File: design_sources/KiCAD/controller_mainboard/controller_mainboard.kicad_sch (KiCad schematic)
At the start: 34 parts, among them J1 XT-90, J10 01x08_2.54mm _socket, J11 2P_screw_term, J12 2P_screw_term, J13 2P_screw_term, J14 2P_screw_term, J2 XT-60, J24 XT-60, J25 XT-60, J3 USB_C_Receptacle_USB2.0_16P, J4 01x08_2.54mm _socket, J5 01x08_2.54mm _socket, J6 01x08_2.54mm _socket, J7 02x18_2.54mm_socket, J8 Conn_01x10_2.54mm_socket, J9 01x08_2.54mm _socket, Q1 2N7002, U12 USBLC6-4SC6

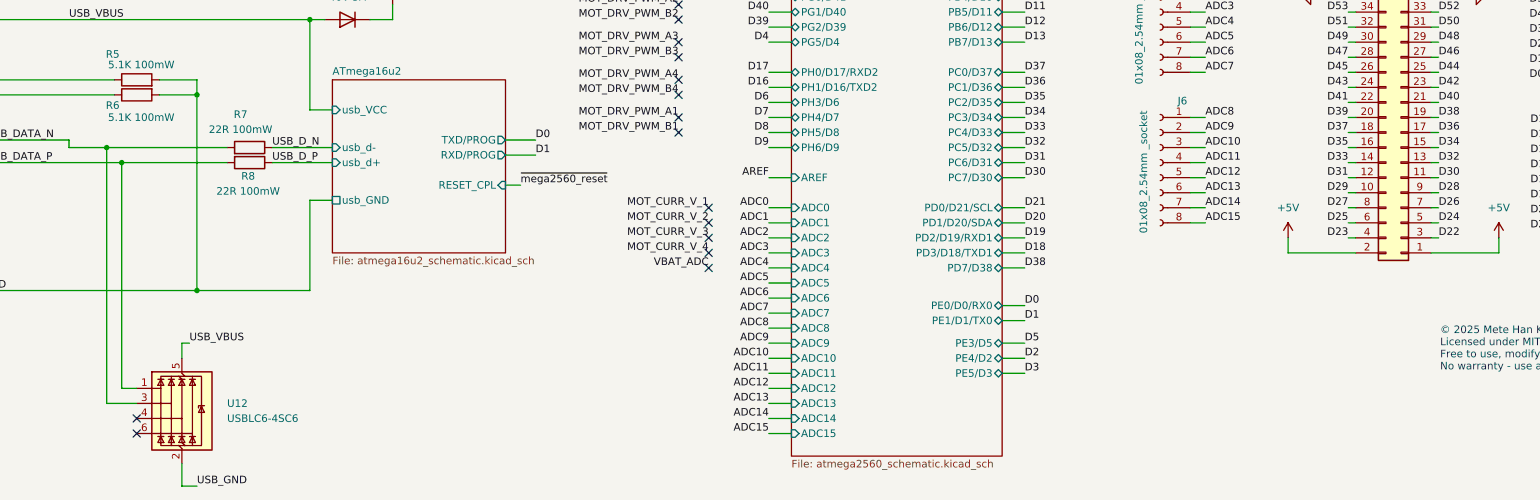
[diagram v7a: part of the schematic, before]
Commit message: Major PCB layout progress, motor drivers are routed and placed. PCB dimensions set, started ATMEGA2560 layout. Slight schematic fixes.
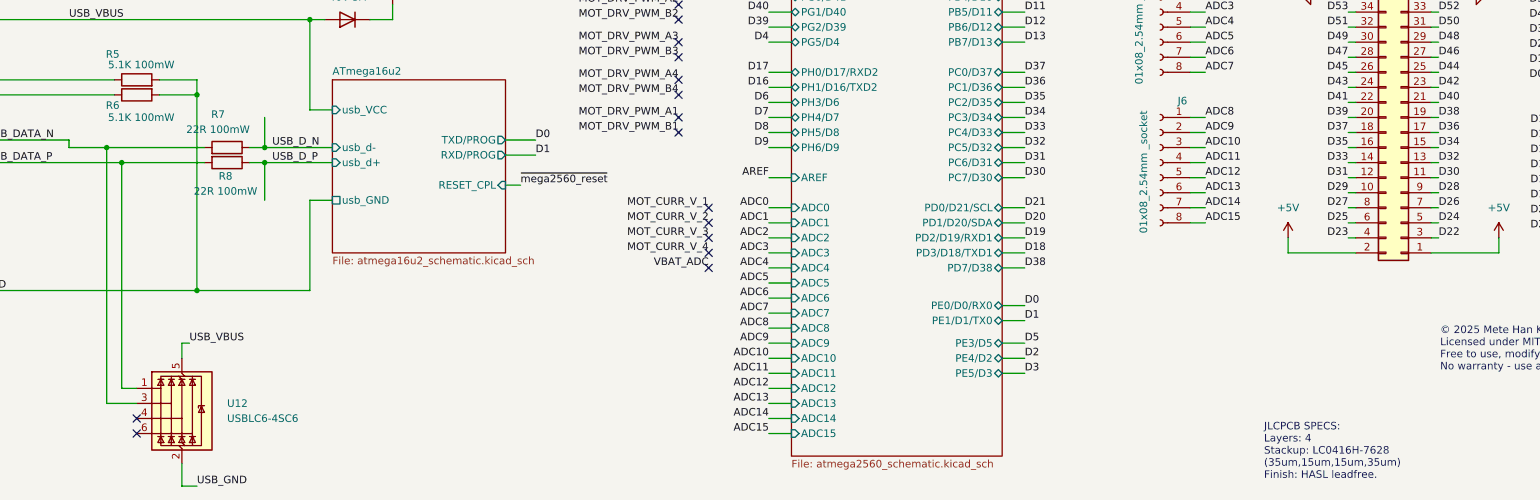
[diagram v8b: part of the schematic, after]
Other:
- note added: "JLCPCB SPECS: Layers: 4 Stackup: LC0416H-7628 (35um,15um,15um,35um) Finish: HASL leadfree."
- moved on the sheet: R7, R8
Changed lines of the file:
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@@
 		)
 	)
+	(text "JLCPCB SPECS:\nLayers: 4 \nStackup: LC0416H-7628\n(35um,15um,15um,35um)\nFinish: HASL leadfree."
+		(exclude_from_sim no)
+		(at 270.256 261.112 0)
+		(effects
+			(font
+				(size 1.27 1.27)
+			)
+			(justify left top)
+		)
+	)
 	(text "Emergency stop\nconnector"
 		(exclude_from_sim no)
@@
 	)
 	(junction
+		(at 101.6 214.63)
+		(diameter 0)
+		(color 0 0 0 0)
+	)
+	(junction
 		(at 90.17 238.76)
 		(diameter 0)
@@
 	)
 	(junction
+		(at 101.6 217.17)
+		(diameter 0)
+		(color 0 0 0 0)
+	)
+	(junction
 		(at 271.78 168.91)
 		(diameter 0)
@@
 	(wire
 		(pts
-			(xy 77.47 217.17) (xy 95.25 217.17)
+			(xy 77.47 217.17) (xy 91.44 217.17)
 		)
 		(stroke
@@
 	(wire
 		(pts
-			(xy 102.87 214.63) (xy 113.03 214.63)
+			(xy 101.6 214.63) (xy 113.03 214.63)
 		)
 		(stroke
@@
 	(wire
 		(pts
+			(xy 101.6 217.17) (xy 113.03 217.17)
+		)
+		(stroke
+			(width 0)
+			(type default)
+		)
+	)
+	(wire
+		(pts
 			(xy 306.07 38.1) (xy 309.88 38.1)
 		)
@@
 	(wire
 		(pts
+			(xy 101.6 209.55) (xy 101.6 214.63)
+		)
+		(stroke
+			(width 0)
+			(type default)
+		)
+	)
+	(wire
+		(pts
 			(xy 29.21 236.22) (xy 29.21 247.65)
 		)
@@
 	(wire
 		(pts
-			(xy 102.87 217.17) (xy 113.03 217.17)
+			(xy 229.87 214.63) (xy 226.06 214.63)
 		)
 		(stroke
@@
 	(wire
 		(pts
-			(xy 229.87 214.63) (xy 226.06 214.63)
+			(xy 186.69 214.63) (xy 190.5 214.63)
 		)
 		(stroke
@@
 	(wire
 		(pts
-			(xy 186.69 214.63) (xy 190.5 214.63)
+			(xy 318.77 173.99) (xy 321.31 173.99)
 		)
 		(stroke
@@
 	(wire
 		(pts
-			(xy 318.77 173.99) (xy 321.31 173.99)
+			(xy 99.06 214.63) (xy 101.6 214.63)
 		)
 		(stroke
@@
 	(wire
 		(pts
+			(xy 99.06 217.17) (xy 101.6 217.17)
+		)
+		(stroke
+			(width 0)
+			(type default)
+		)
+	)
+	(wire
+		(pts
 			(xy 203.2 44.45) (xy 207.01 44.45)
 		)
@@
 	(wire
 		(pts
-			(xy 74.93 214.63) (xy 95.25 214.63)
+			(xy 74.93 214.63) (xy 91.44 214.63)
 		)
 		(stroke
@@
 	(wire
 		(pts
+			(xy 101.6 223.52) (xy 101.6 217.17)
+		)
+		(stroke
+			(width 0)
+			(type default)
+		)
+	)
+	(wire
+		(pts
 			(xy 229.87 212.09) (xy 226.06 212.09)
 		)
@@
 		)
 	)
+	(netclass_flag ""
+		(length 2.54)
+		(shape round)
+		(at 101.6 209.55 0)
+		(fields_autoplaced yes)
+		(effects
+			(font
+				(size 1.27 1.27)
+			)
+			(justify left bottom)
+		)
+		(property "Netclass" "USB_differential"
+			(at 100.9015 207.01 0)
+			(effects
+				(font
+					(size 1.27 1.27)
+				)
+				(justify right)
+			)
+		)
+		(property "Component Class" ""
+			(at 236.22 13.97 0)
+			(effects
+				(font
+					(size 1.27 1.27)
+					(italic yes)
+				)
+				(justify left)
+			)
+		)
+	)
+	(netclass_flag ""
+		(length 2.54)
+		(shape round)
+		(at 69.85 217.17 180)
+		(fields_autoplaced yes)
+		(effects
+			(font
+				(size 1.27 1.27)
+			)
+			(justify right bottom)
+		)
+		(property "Netclass" "USB_differential"
+			(at 70.5485 219.71 0)
+			(effects
+				(font
+					(size 1.27 1.27)
+				)
+				(justify left)
+			)
+		)
+		(property "Component Class" ""
+			(at -64.77 21.59 0)
+			(effects
+				(font
+					(size 1.27 1.27)
+					(italic yes)
+				)
+				(justify right)
+			)
+		)
+	)
+	(netclass_flag ""
+		(length 2.54)
+		(shape round)
+		(at 101.6 223.52 180)
+		(fields_autoplaced yes)
+		(effects
+			(font
+				(size 1.27 1.27)
+			)
+			(justify right bottom)
+		)
+		(property "Netclass" "USB_differential"
+			(at 100.9015 226.06 0)
+			(effects
+				(font
+					(size 1.27 1.27)
+				)
+				(justify right)
+			)
+		)
+		(property "Component Class" ""
+			(at -33.02 27.94 0)
+			(effects
+				(font
+					(size 1.27 1.27)
+					(italic yes)
+				)
+				(justify right)
+			)
+		)
+	)
+	(netclass_flag ""
+		(length 2.54)
+		(shape round)
+		(at 69.85 214.63 0)
+		(fields_autoplaced yes)
+		(effects
+			(font
+				(size 1.27 1.27)
+			)
+			(justify left bottom)
+		)
+		(property "Netclass" "USB_differential"
+			(at 70.5485 212.09 0)
+			(effects
+				(font
+					(size 1.27 1.27)
+				)
+				(justify left)
+			)
+		)
+		(property "Component Class" ""
+			(at -64.77 19.05 0)
+			(effects
+				(font
+					(size 1.27 1.27)
+					(italic yes)
+				)
+			)
+		)
+	)
 	(symbol
 		(lib_id "Device:R")
@@
 	(symbol
 		(lib_id "Device:R")
-		(at 99.06 214.63 270)
+		(at 95.25 214.63 270)
 		(mirror x)
 		(unit 1)
@@
 		(dnp no)
 		(property "Reference" "R7"
-			(at 97.536 209.042 90)
+			(at 93.726 209.042 90)
 			(effects
 				(font
@@
 		)
 		(property "Value" "22R 100mW"
-			(at 97.536 211.582 90)
+			(at 93.726 211.582 90)
 			(effects
 				(font
@@
 		)
 		(property "Footprint" "Resistor_SMD:R_0603_1608Metric"
-			(at 99.06 216.408 90)
+			(at 95.25 216.408 90)
 			(effects
 				(font
@@
 		)
 		(property "Datasheet" "~"
-			(at 99.06 214.63 0)
+			(at 95.25 214.63 0)
 			(effects
 				(font
@@
 		)
 		(property "Description" "Resistor"
-			(at 99.06 214.63 0)
+			(at 95.25 214.63 0)
 			(effects
 				(font
@@
 		)
 		(property "JLCPCB" "C23345"
-			(at 99.06 214.63 0)
+			(at 95.25 214.63 0)
 			(effects
 				(font
@@
 	(symbol
 		(lib_id "Device:R")
-		(at 99.06 217.17 270)
+		(at 95.25 217.17 270)
 		(unit 1)
 		(exclude_from_sim no)
@@
 		(dnp no)
 		(property "Reference" "R8"
-			(at 98.806 219.456 90)
+			(at 94.996 219.456 90)
 			(effects
 				(font
@@
 		)
 		(property "Value" "22R 100mW"
-			(at 98.806 221.996 90)
+			(at 94.996 221.996 90)
 			(effects
 				(font
@@
 		)
 		(property "Footprint" "Resistor_SMD:R_0603_1608Metric"
-			(at 99.06 215.392 90)
+			(at 95.25 215.392 90)
 			(effects
 				(font
@@
 		)
 		(property "Datasheet" "~"
-			(at 99.06 217.17 0)
+			(at 95.25 217.17 0)
 			(effects
 				(font
@@
 		)
 		(property "Description" "Resistor"
-			(at 99.06 217.17 0)
+			(at 95.25 217.17 0)
 			(effects
 				(font
@@
 		)
 		(property "JLCPCB" "C23345"
-			(at 99.06 217.17 0)
+			(at 95.25 217.17 0)
 			(effects
 				(font
